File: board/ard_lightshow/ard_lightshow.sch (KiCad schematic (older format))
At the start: 5 parts, among them U0 arduino_nano, U1 rf24, U2 mic_electret

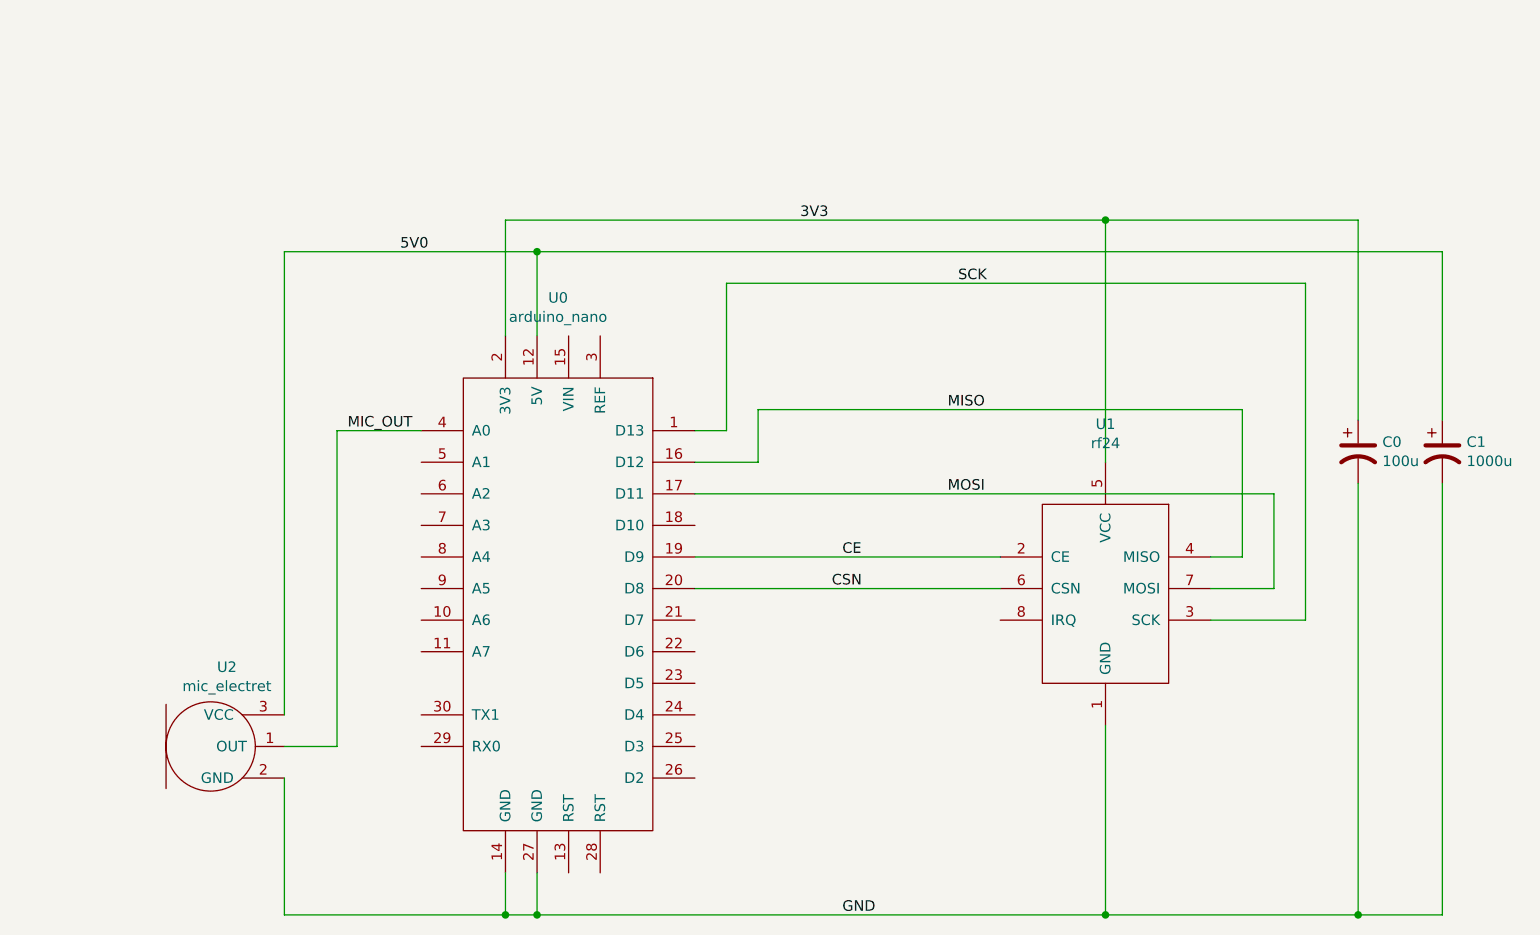
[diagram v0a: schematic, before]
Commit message: Swapped to a single PCB with 0402 SMD resistors that can be solder jumped for either configuration.
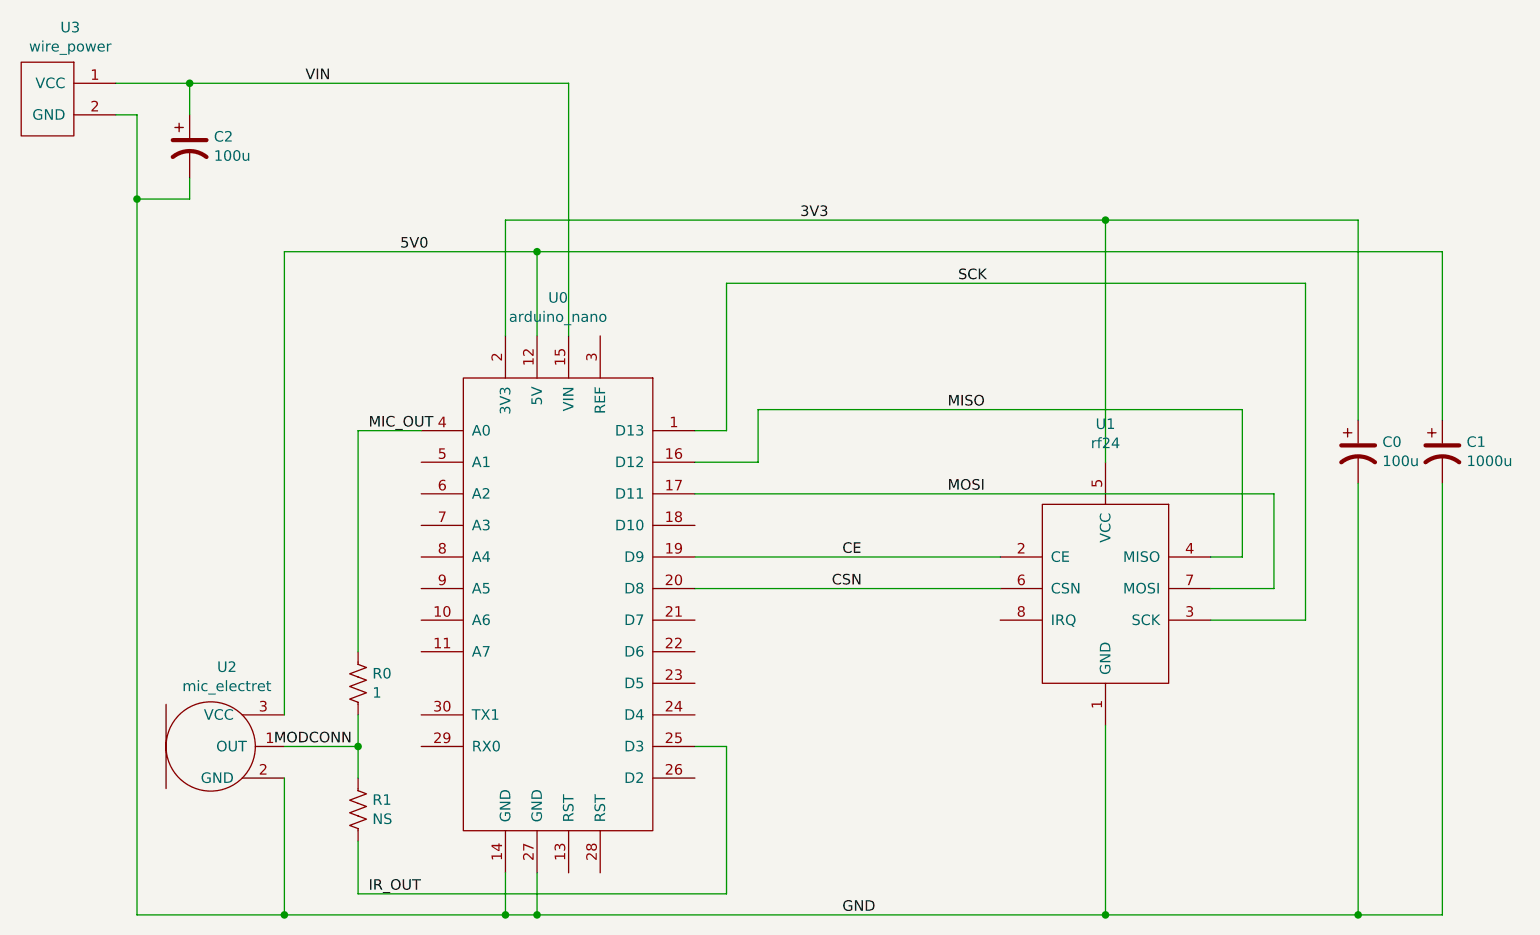
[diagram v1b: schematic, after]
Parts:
- added C2: 100u, Capacitors_THT:CP_Radial_D5.0mm_P2.50mm, symbol Device:CP1
- added R0: 1, Resistors_SMD:R_0402, symbol Device:R_US
- added R1: NS, Resistors_SMD:R_0402, symbol Device:R_US
- added U3: wire_power, custom_arduino:wire_power, symbol custom_arduino:wire_power
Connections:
- net GND: now also C2.2, U3.2 (GND)
- net MIC_OUT: now also R0.1; no longer U2.1 (OUT)
- net VIN: now reaches U0.15 (VIN)
- net VIN: now also C2.1, U3.1 (VCC)
- net IR_OUT: now reaches U0.25 (D3)
- net IR_OUT: now also R1.2
- new net: R0.2, R1.1, U2.1 (OUT)
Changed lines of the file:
@@
 $EndDescr
-Wire Wire Line
-	3800 3100 3400 3100
-Wire Wire Line
-	3400 3100 3400 4600
-Wire Wire Line
-	3400 4600 3150 4600
 Wire Wire Line
 	3150 4450 3150 2250
@@
 Text Label 5800 5400 0    50   ~ 0
 GND
-Text Label 3450 3100 0    50   ~ 0
+Text Label 3550 3100 0    50   ~ 0
 MIC_OUT
 $Comp
@@
 	-1   0    0    -1
 $EndComp
+$Comp
+L custom_arduino:wire_power U3
+U 1 1 5FB588F3
+P 2350 1700
+F 0 "U3" H 2567 2215 50  0000 C CNN
+F 1 "wire_power" H 2567 2124 50  0000 C CNN
+F 2 "custom_arduino:wire_power" H 2850 1850 50  0001 C CNN
+F 3 "" H 2850 1850 50  0001 C CNN
+	1    2350 1700
+	-1   0    0    -1
+$EndComp
+Wire Wire Line
+	3150 5400 2450 5400
+Wire Wire Line
+	2450 5400 2450 2000
+Wire Wire Line
+	2450 1600 2350 1600
+Connection ~ 3150 5400
+Wire Wire Line
+	2350 1450 2700 1450
+Wire Wire Line
+	4500 1450 4500 2650
+Text Label 3250 1450 0    50   ~ 0
+VIN
+$Comp
+L Device:CP1 C2
+U 1 1 5FB5A700
+P 2700 1750
+F 0 "C2" H 2815 1796 50  0000 L CNN
+F 1 "100u" H 2815 1705 50  0000 L CNN
+F 2 "Capacitors_THT:CP_Radial_D5.0mm_P2.50mm" H 2700 1750 50  0001 C CNN
+F 3 "~" H 2700 1750 50  0001 C CNN
+	1    2700 1750
+	1    0    0    -1
+$EndComp
+Wire Wire Line
+	2700 1600 2700 1450
+Connection ~ 2700 1450
+Wire Wire Line
+	2700 1450 4500 1450
+Wire Wire Line
+	2700 1900 2700 2000
+Wire Wire Line
+	2700 2000 2450 2000
+Connection ~ 2450 2000
+Wire Wire Line
+	2450 2000 2450 1600
+$Comp
+L Device:R_US R0
+U 1 1 5FB5A89E
+P 3500 4300
+F 0 "R0" H 3568 4346 50  0000 L CNN
+F 1 "1" H 3568 4255 50  0000 L CNN
+F 2 "Resistors_SMD:R_0402" V 3540 4290 50  0001 C CNN
+F 3 "~" H 3500 4300 50  0001 C CNN
+	1    3500 4300
+	1    0    0    -1
+$EndComp
+$Comp
+L Device:R_US R1
+U 1 1 5FB5B7C3
+P 3500 4900
+F 0 "R1" H 3568 4946 50  0000 L CNN
+F 1 "NS" H 3568 4855 50  0000 L CNN
+F 2 "Resistors_SMD:R_0402" V 3540 4890 50  0001 C CNN
+F 3 "~" H 3500 4900 50  0001 C CNN
+	1    3500 4900
+	1    0    0    -1
+$EndComp
+Wire Wire Line
+	3500 4450 3500 4600
+Connection ~ 3500 4600
+Wire Wire Line
+	3500 4600 3500 4750
+Wire Wire Line
+	3500 5050 3500 5300
+Wire Wire Line
+	3500 5300 5250 5300
+Wire Wire Line
+	5250 5300 5250 4600
+Wire Wire Line
+	5250 4600 5100 4600
+Wire Wire Line
+	3500 3100 3500 4150
+Text Label 3550 5300 0    50   ~ 0
+IR_OUT
+Text Label 3100 4600 0    50   ~ 0
+MODCONN
+Wire Wire Line
+	3800 3100 3500 3100
+Wire Wire Line
+	3150 4600 3500 4600
 $EndSCHEMATC

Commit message: Bumped up isolation and decals/solder mask to aid in micro-batch CNC milling.
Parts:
- R0, R1: footprint Resistors_SMD:R_0402 -> Resistors_SMD:R_0805
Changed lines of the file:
@@
 F 0 "R0" H 3568 4346 50  0000 L CNN
 F 1 "1" H 3568 4255 50  0000 L CNN
-F 2 "Resistors_SMD:R_0402" V 3540 4290 50  0001 C CNN
+F 2 "Resistors_SMD:R_0805" V 3540 4290 50  0001 C CNN
 F 3 "~" H 3500 4300 50  0001 C CNN
 	1    3500 4300
@@
 F 0 "R1" H 3568 4946 50  0000 L CNN
 F 1 "NS" H 3568 4855 50  0000 L CNN
-F 2 "Resistors_SMD:R_0402" V 3540 4890 50  0001 C CNN
+F 2 "Resistors_SMD:R_0805" V 3540 4890 50  0001 C CNN
 F 3 "~" H 3500 4900 50  0001 C CNN
 	1    3500 4900
